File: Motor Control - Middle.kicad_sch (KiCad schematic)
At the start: 0 parts

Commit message: Update Schematic
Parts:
- added C52: 4.7uF 16V 0402, Duc_Library:C0402, symbol Duc-Capacitors:CAP CER 0402
- added C53: 100nF 16V 0603, Duc_Library:C0402, symbol Duc-Capacitors:CAP CER 0402
- added C54: 100nF 16V 0402, Duc_Library:C0402, symbol Duc-Capacitors:CAP CER 0402
- added C55: 470nF 16V 0402, Duc_Library:C0402, symbol Duc-Capacitors:CAP CER 0402
- added J3: BM09B-SRSS-TB, Duc:CONN-SMD_9P-P1.00_BM09B-SRSS-TB, symbol Duc-Connectors:BM09B-SRSS-TB
- added R10: 1R 0.1% 0402, Duc_Library:R0402, symbol Duc-Resistors:RES SMD 0402
- added R11: 10K 0.1% 0402, Duc_Library:R0402, symbol Duc-Resistors:RES SMD 0402
- added R12: 510R 0.1% 0402, Duc_Library:R0402, symbol Duc-Resistors:RES SMD 0402
- added U11: TB9051FTG,EL, Duc_Library:UQFN-28_L6.0-W6.0-P0.65-BL-EP4.0, symbol Duc-ICs:TB9051FTG,EL
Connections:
- new net +3.3V: J3.3, J3.8
- new net +5V: C52.2, J3.10, J3.11, R10.1
- new net +VBAT: C54.2, U11.11 (VBAT), U11.12 (VBAT), U11.24 (VBAT), U11.25 (VBAT)
- new net DGND: C52.1, C53.1, C55.1, R12.2, U11.1 (OCC), U11.27 (TEST1), U11.28 (TEST2), U11.3 (ENB), U11.4 (AGND)
- new net DIAG_M: U11.18 (DIAG)
- new net ECA_M: J3.6
- new net ECB_M: J3.7
- new net ECC_M: J3.2
- new net EN_M: U11.5 (EN)
- new net GND: C54.1, J3.1, J3.5, U11.15 (PGND), U11.16 (PGND), U11.17 (PGND), U11.19 (PGND), U11.20 (PGND), U11.21 (PGND), U11.29 (EP)
- new net OCM_M: R11.1, R12.1
- new net OUT1_M: J3.4, U11.13 (OUT1), U11.14 (OUT1)
- new net OUT2_M: J3.9, U11.22 (OUT2), U11.23 (OUT2)
- new net PWMA_M: U11.8 (PWM1)
- new net PWMB_M: U11.9 (PWM2)
- new net VCC_M: C53.2, R10.2, U11.2 (VCC)
- new net _OCM_M: C55.2, R11.2, U11.7 (OCM)
- no-connect marks 0 -> 3

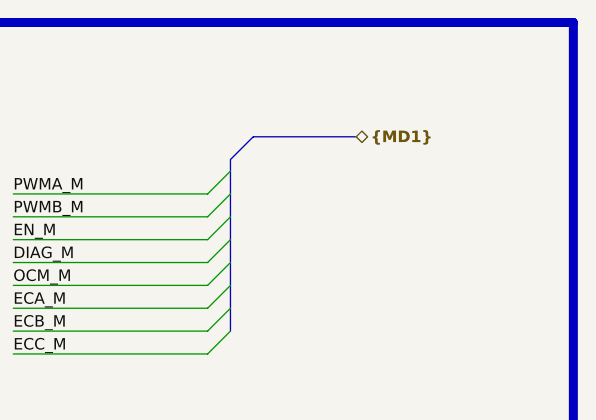
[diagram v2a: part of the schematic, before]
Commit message: Update Motor Schematic
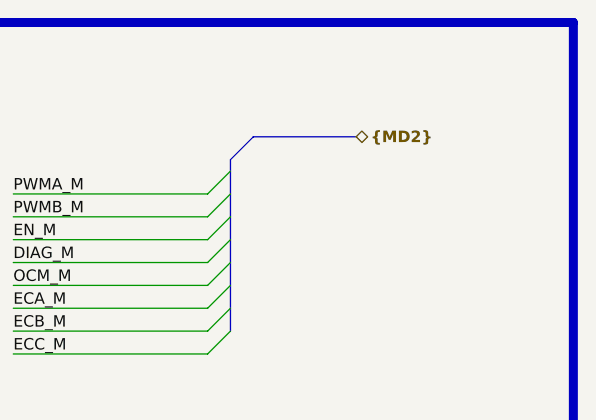
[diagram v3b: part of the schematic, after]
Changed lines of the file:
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@@
 		)
 	)
-	(hierarchical_label "{MD1}"
+	(hierarchical_label "{MD2}"
 		(shape bidirectional)
 		(at 229.87 38.1 0)
@@
 		(instances
 			(project "Master_Hand_Kicad"
-				(path "/f9e05184-c88b-4a88-ae9c-ab2bdb32be7c/c5103ceb-5325-4a84-a025-9638a412984e/62e1134a-4afa-47e5-8a81-2f23b9b85122/d22c5670-9da0-4f2f-acb0-4fbe9e5abdf2"
+				(path "/f9e05184-c88b-4a88-ae9c-ab2bdb32be7c/c5103ceb-5325-4a84-a025-9638a412984e/d622f5b6-19d6-40b1-8c69-868393d4ee00"
 					(reference "#PWR038")
 					(unit 1)
@@
 		(instances
 			(project "Master_Hand_Kicad"
-				(path "/f9e05184-c88b-4a88-ae9c-ab2bdb32be7c/c5103ceb-5325-4a84-a025-9638a412984e/62e1134a-4afa-47e5-8a81-2f23b9b85122/d22c5670-9da0-4f2f-acb0-4fbe9e5abdf2"
+				(path "/f9e05184-c88b-4a88-ae9c-ab2bdb32be7c/c5103ceb-5325-4a84-a025-9638a412984e/d622f5b6-19d6-40b1-8c69-868393d4ee00"
 					(reference "#PWR044")
 					(unit 1)
@@
 		(instances
 			(project "Master_Hand_Kicad"
-				(path "/f9e05184-c88b-4a88-ae9c-ab2bdb32be7c/c5103ceb-5325-4a84-a025-9638a412984e/62e1134a-4afa-47e5-8a81-2f23b9b85122/d22c5670-9da0-4f2f-acb0-4fbe9e5abdf2"
+				(path "/f9e05184-c88b-4a88-ae9c-ab2bdb32be7c/c5103ceb-5325-4a84-a025-9638a412984e/d622f5b6-19d6-40b1-8c69-868393d4ee00"
 					(reference "#PWR040")
 					(unit 1)
@@
 		(instances
 			(project "Master_Hand_Kicad"
-				(path "/f9e05184-c88b-4a88-ae9c-ab2bdb32be7c/c5103ceb-5325-4a84-a025-9638a412984e/62e1134a-4afa-47e5-8a81-2f23b9b85122/d22c5670-9da0-4f2f-acb0-4fbe9e5abdf2"
+				(path "/f9e05184-c88b-4a88-ae9c-ab2bdb32be7c/c5103ceb-5325-4a84-a025-9638a412984e/d622f5b6-19d6-40b1-8c69-868393d4ee00"
 					(reference "R12")
 					(unit 1)
@@
 		(instances
 			(project "Master_Hand_Kicad"
-				(path "/f9e05184-c88b-4a88-ae9c-ab2bdb32be7c/c5103ceb-5325-4a84-a025-9638a412984e/62e1134a-4afa-47e5-8a81-2f23b9b85122/d22c5670-9da0-4f2f-acb0-4fbe9e5abdf2"
+				(path "/f9e05184-c88b-4a88-ae9c-ab2bdb32be7c/c5103ceb-5325-4a84-a025-9638a412984e/d622f5b6-19d6-40b1-8c69-868393d4ee00"
 					(reference "J3")
 					(unit 1)
@@
 		(instances
 			(project "Master_Hand_Kicad"
-				(path "/f9e05184-c88b-4a88-ae9c-ab2bdb32be7c/c5103ceb-5325-4a84-a025-9638a412984e/62e1134a-4afa-47e5-8a81-2f23b9b85122/d22c5670-9da0-4f2f-acb0-4fbe9e5abdf2"
+				(path "/f9e05184-c88b-4a88-ae9c-ab2bdb32be7c/c5103ceb-5325-4a84-a025-9638a412984e/d622f5b6-19d6-40b1-8c69-868393d4ee00"
 					(reference "C54")
 					(unit 1)
@@
 		(instances
 			(project "Master_Hand_Kicad"
-				(path "/f9e05184-c88b-4a88-ae9c-ab2bdb32be7c/c5103ceb-5325-4a84-a025-9638a412984e/62e1134a-4afa-47e5-8a81-2f23b9b85122/d22c5670-9da0-4f2f-acb0-4fbe9e5abdf2"
+				(path "/f9e05184-c88b-4a88-ae9c-ab2bdb32be7c/c5103ceb-5325-4a84-a025-9638a412984e/d622f5b6-19d6-40b1-8c69-868393d4ee00"
 					(reference "#PWR045")
 					(unit 1)
@@
 		(instances
 			(project "Master_Hand_Kicad"
-				(path "/f9e05184-c88b-4a88-ae9c-ab2bdb32be7c/c5103ceb-5325-4a84-a025-9638a412984e/62e1134a-4afa-47e5-8a81-2f23b9b85122/d22c5670-9da0-4f2f-acb0-4fbe9e5abdf2"
+				(path "/f9e05184-c88b-4a88-ae9c-ab2bdb32be7c/c5103ceb-5325-4a84-a025-9638a412984e/d622f5b6-19d6-40b1-8c69-868393d4ee00"
 					(reference "C55")
 					(unit 1)
@@
 		(instances
 			(project "Master_Hand_Kicad"
-				(path "/f9e05184-c88b-4a88-ae9c-ab2bdb32be7c/c5103ceb-5325-4a84-a025-9638a412984e/62e1134a-4afa-47e5-8a81-2f23b9b85122/d22c5670-9da0-4f2f-acb0-4fbe9e5abdf2"
+				(path "/f9e05184-c88b-4a88-ae9c-ab2bdb32be7c/c5103ceb-5325-4a84-a025-9638a412984e/d622f5b6-19d6-40b1-8c69-868393d4ee00"
 					(reference "#PWR042")
 					(unit 1)
@@
 		(instances
 			(project "Master_Hand_Kicad"
-				(path "/f9e05184-c88b-4a88-ae9c-ab2bdb32be7c/c5103ceb-5325-4a84-a025-9638a412984e/62e1134a-4afa-47e5-8a81-2f23b9b85122/d22c5670-9da0-4f2f-acb0-4fbe9e5abdf2"
+				(path "/f9e05184-c88b-4a88-ae9c-ab2bdb32be7c/c5103ceb-5325-4a84-a025-9638a412984e/d622f5b6-19d6-40b1-8c69-868393d4ee00"
 					(reference "U11")
 					(unit 1)
@@
 		(instances
 			(project "Master_Hand_Kicad"
-				(path "/f9e05184-c88b-4a88-ae9c-ab2bdb32be7c/c5103ceb-5325-4a84-a025-9638a412984e/62e1134a-4afa-47e5-8a81-2f23b9b85122/d22c5670-9da0-4f2f-acb0-4fbe9e5abdf2"
+				(path "/f9e05184-c88b-4a88-ae9c-ab2bdb32be7c/c5103ceb-5325-4a84-a025-9638a412984e/d622f5b6-19d6-40b1-8c69-868393d4ee00"
 					(reference "C53")
 					(unit 1)
@@
 		(instances
 			(project "Master_Hand_Kicad"
-				(path "/f9e05184-c88b-4a88-ae9c-ab2bdb32be7c/c5103ceb-5325-4a84-a025-9638a412984e/62e1134a-4afa-47e5-8a81-2f23b9b85122/d22c5670-9da0-4f2f-acb0-4fbe9e5abdf2"
+				(path "/f9e05184-c88b-4a88-ae9c-ab2bdb32be7c/c5103ceb-5325-4a84-a025-9638a412984e/d622f5b6-19d6-40b1-8c69-868393d4ee00"
 					(reference "#PWR041")
 					(unit 1)
@@
 		(instances
 			(project "Master_Hand_Kicad"
-				(path "/f9e05184-c88b-4a88-ae9c-ab2bdb32be7c/c5103ceb-5325-4a84-a025-9638a412984e/62e1134a-4afa-47e5-8a81-2f23b9b85122/d22c5670-9da0-4f2f-acb0-4fbe9e5abdf2"
+				(path "/f9e05184-c88b-4a88-ae9c-ab2bdb32be7c/c5103ceb-5325-4a84-a025-9638a412984e/d622f5b6-19d6-40b1-8c69-868393d4ee00"
 					(reference "C52")
 					(unit 1)
@@
 		(instances
 			(project "Master_Hand_Kicad"
-				(path "/f9e05184-c88b-4a88-ae9c-ab2bdb32be7c/c5103ceb-5325-4a84-a025-9638a412984e/62e1134a-4afa-47e5-8a81-2f23b9b85122/d22c5670-9da0-4f2f-acb0-4fbe9e5abdf2"
+				(path "/f9e05184-c88b-4a88-ae9c-ab2bdb32be7c/c5103ceb-5325-4a84-a025-9638a412984e/d622f5b6-19d6-40b1-8c69-868393d4ee00"
 					(reference "#PWR043")
 					(unit 1)
@@
 		(instances
 			(project "Master_Hand_Kicad"
-				(path "/f9e05184-c88b-4a88-ae9c-ab2bdb32be7c/c5103ceb-5325-4a84-a025-9638a412984e/62e1134a-4afa-47e5-8a81-2f23b9b85122/d22c5670-9da0-4f2f-acb0-4fbe9e5abdf2"
+				(path "/f9e05184-c88b-4a88-ae9c-ab2bdb32be7c/c5103ceb-5325-4a84-a025-9638a412984e/d622f5b6-19d6-40b1-8c69-868393d4ee00"
 					(reference "#PWR039")
 					(unit 1)
@@
 		(instances
 			(project "Master_Hand_Kicad"
-				(path "/f9e05184-c88b-4a88-ae9c-ab2bdb32be7c/c5103ceb-5325-4a84-a025-9638a412984e/62e1134a-4afa-47e5-8a81-2f23b9b85122/d22c5670-9da0-4f2f-acb0-4fbe9e5abdf2"
+				(path "/f9e05184-c88b-4a88-ae9c-ab2bdb32be7c/c5103ceb-5325-4a84-a025-9638a412984e/d622f5b6-19d6-40b1-8c69-868393d4ee00"
 					(reference "R11")
 					(unit 1)
@@
 		(instances
 			(project "Master_Hand_Kicad"
-				(path "/f9e05184-c88b-4a88-ae9c-ab2bdb32be7c/c5103ceb-5325-4a84-a025-9638a412984e/62e1134a-4afa-47e5-8a81-2f23b9b85122/d22c5670-9da0-4f2f-acb0-4fbe9e5abdf2"
+				(path "/f9e05184-c88b-4a88-ae9c-ab2bdb32be7c/c5103ceb-5325-4a84-a025-9638a412984e/d622f5b6-19d6-40b1-8c69-868393d4ee00"
 					(reference "R10")
 					(unit 1)

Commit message: Update Schematic
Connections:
- net DGND is gone; now on net GND: C52.1, C53.1, C55.1, R12.2, U11.1 (OCC), U11.27 (TEST1), U11.28 (TEST2), U11.3 (ENB), U11.4 (AGND)

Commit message: Update Schematic
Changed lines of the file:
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@@
+		)
+	)
+	(rectangle
+		(start 177.8 25.4)
+		(end 254 76.2)
+		(stroke
+			(width 1)
+			(type default)
+			(color 200 0 0 1)
+		)
+		(fill
+			(type none)
 		)
 	)

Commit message: Update Schematic
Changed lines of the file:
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@@
-	)
-	(junction
-		(at 147.32 66.04)
-		(diameter 0)
-		(color 0 0 0 0)
 	)
 	(junction
@@
 	(junction
 		(at 66.04 129.54)
+		(diameter 0)
+		(color 0 0 0 0)
+	)
+	(junction
+		(at 148.59 66.04)
 		(diameter 0)
 		(color 0 0 0 0)
@@
 	(wire
 		(pts
-			(xy 137.16 66.04) (xy 147.32 66.04)
+			(xy 137.16 66.04) (xy 148.59 66.04)
 		)
 		(stroke
@@
 	(wire
 		(pts
-			(xy 147.32 63.5) (xy 147.32 66.04)
+			(xy 148.59 63.5) (xy 148.59 66.04)
 		)
 		(stroke
@@
 	(wire
 		(pts
-			(xy 147.32 66.04) (xy 160.02 66.04)
-		)
-		(stroke
-			(width 0)
-			(type default)
-		)
-	)
-	(wire
-		(pts
 			(xy 88.9 127) (xy 88.9 129.54)
 		)
@@
 	(wire
 		(pts
+			(xy 148.59 66.04) (xy 160.02 66.04)
+		)
+		(stroke
+			(width 0)
+			(type default)
+		)
+	)
+	(wire
+		(pts
 			(xy 231.14 119.38) (xy 234.95 119.38)
 		)
@@
 	(wire
 		(pts
-			(xy 137.16 63.5) (xy 147.32 63.5)
-		)
-		(stroke
+			(xy 137.16 63.5) (xy 148.59 63.5)
+		)
+		(stroke

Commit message: Update Schematic
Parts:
- removed J3: BM09B-SRSS-TB, Duc:CONN-SMD_9P-P1.00_BM09B-SRSS-TB, symbol Duc-Connectors:BM09B-SRSS-TB
- added C88, C89: 100nF 16V 0402, Duc_Library:C0402, symbol Duc-Capacitors:CAP CER 0402
- added J4: BM09B-SRSS-TB, Duc:CONN-SMD_9P-P1.00_BM09B-SRSS-TB, symbol Duc-Connectors:BM09B-SRSS-TB
- added R59, R72: 220R 0.1% 0402, Duc_Library:R0402, symbol Duc-Resistors:RES SMD 0402
- added R60: 1K 0.1% 0402, Duc_Library:R0402, symbol Duc-Resistors:RES SMD 0402
- R11: value 10K 0.1% 0402 -> 1K 0.1% 0402
- R12: value 510R 0.1% 0402 -> 220R 0.1% 0402
- renumbered U11 to U9
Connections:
- net DIAG_M: now also R59.2; no longer U9.18 (DIAG)
- net ECA_M: now also J4.6
- net ECB_M: now also J4.7
- net ECC_M: now also C89.2, R72.2
- net GND: now also C88.1, C89.1, J4.1, J4.10, J4.11, J4.5
- net OUT1_M: now also J4.4
- net OUT2_M: now also J4.9
- new net +3V3: J4.8, R60.2
- new net +A3V3: C88.2, J4.3
- new net _DIAG_M: R59.1, R60.1, U9.18 (DIAG)
- new net _ECC_M: J4.2, R72.1
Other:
- moved on the sheet: C52, C53, C54, C55, R10, R11, R12

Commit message: Update Schematic
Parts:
- renumbered C52 to C58, C53 to C59, C54 to C60, C55 to C61, C88 to C62, C89 to C63, R10 to R13, R11 to R14, R59 to R15, R12 to R16, R60 to R17, R72 to R18
